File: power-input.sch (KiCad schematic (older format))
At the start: 23 parts, among them J301 Conn_01x02, J302 Conn_01x02, J303 Conn_01x02, U301 SY8401

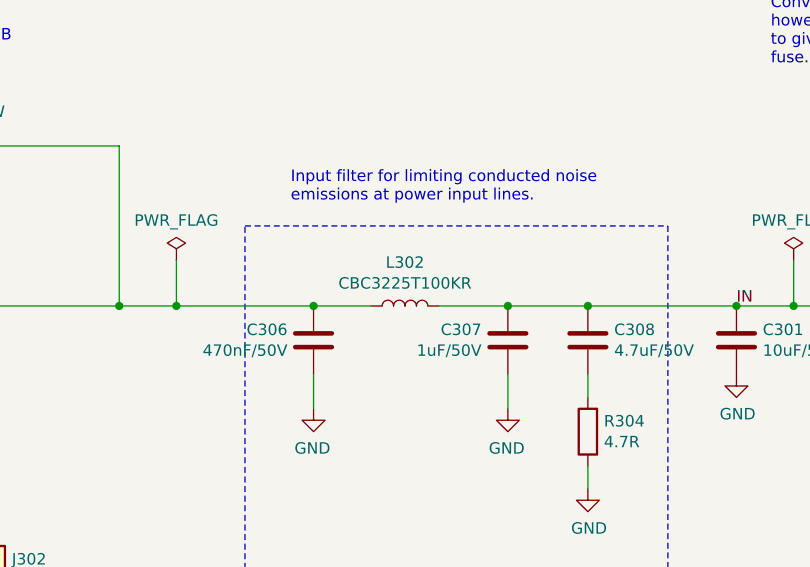
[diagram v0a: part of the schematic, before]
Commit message: Replace L302 for better availability
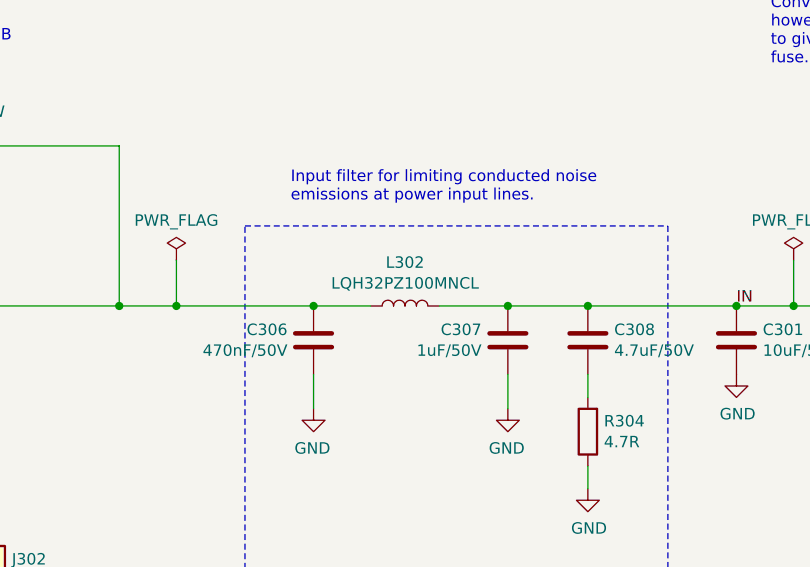
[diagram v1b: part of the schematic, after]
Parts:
- L302: value CBC3225T100KR -> LQH32PZ100MNCL; LCSC C90321 -> C464437; Notes (none) -> Alternative: CBC3225T100KR
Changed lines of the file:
@@
 AR Path="/5F6FAF6E/60159EC7" Ref="L302"  Part="1"
 F 0 "L302" V 4990 4800 50  0000 C CNN
-F 1 "CBC3225T100KR" V 4899 4800 50  0000 C CNN
+F 1 "LQH32PZ100MNCL" V 4899 4800 50  0000 C CNN
 F 2 "Inductor_SMD:L_1210_3225Metric" H 4800 4800 50  0001 C CNN
 F 3 "~" H 4800 4800 50  0001 C CNN
 F 4 "" V 4800 4800 50  0001 C CNN "URL"
 F 5 "" V 4800 4800 50  0001 C CNN "Part"
-F 6 "C90321" H 4800 4800 50  0001 C CNN "LCSC"
+F 6 "C464437" H 4800 4800 50  0001 C CNN "LCSC"
+F 7 "Alternative: CBC3225T100KR" V 4800 4800 50  0001 C CNN "Notes"
 	1    4800 4800
 	0    -1   -1   0

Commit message: Replace buck converter and CAN transceiver ICs
IC substitutions necessitated by component supply issues.
Other changes:
- Buck converter layout changes due to larger peripherals
- Isolated CAN transceiver replaced by separate digital isolators
  and transceivers. Layout changes.
- Changed JST XH conx to easier-to-use Phoenix MCs
- Removed dedicated Vin Prot conx (still available via VLink)
- Removed dedicated GND from left I/O header
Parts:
- removed C303: 100nF, Capacitor_SMD:C_0402_1005Metric, symbol Device:C
- removed C305: 10nF/50V, Capacitor_SMD:C_0402_1005Metric, symbol Device:C
- removed J302: Conn_01x02, Connector_PinHeader_2.54mm:PinHeader_1x02_P2.54mm_Vertical, symbol Connector_Generic:Conn_01x02
- removed J303: Conn_01x02, SH-ESP32:WireLink_1x02_P2.54mm, symbol Connector_Generic:Conn_01x02
- removed U301: SY8401, Package_TO_SOT_SMD:SOT-23-6, symbol SH-ESP32:SY8401
- added C201: 20nF, Capacitor_SMD:C_0402_1005Metric, symbol Device:C
- added J204: Conn_01x02, Connector_PinHeader_2.54mm:PinHeader_1x02_P2.54mm_Vertical, symbol Connector_Generic:Conn_01x02
- added U202: XL1509-ADJE1, Package_SO:SOP-8_3.9x4.9mm_P1.27mm, symbol SH-ESP32:XL1509-ADJE1
- C301: value 10uF/50V -> 22uF/35V; LCSC C13585 -> C342620; Notes 50V -> 35V
- C304: value 22uF/6.3V -> 100uF/6.3V; footprint Capacitor_SMD:C_0805_2012Metric -> Capacitor_SMD:C_1206_3216Metric; LCSC C45783 -> C15008
- D302: value B5819W -> SS24FL; footprint Diode_SMD:D_SOD-123 -> Diode_SMD:D_SOD-123F; LCSC C8598 -> C489144
- J301: footprint Connector_JST:JST_XH_B2B-XH-A_1x02_P2.50mm_Vertical -> Connector_Phoenix_MC:PhoenixContact_MCV_1,5_2-G-3.81_1x02_P3.81mm_Vertical
- L301: value MWSA0503S-100MT -> SMMS0650-470M; footprint Inductor_SMD:L_Sunlord_MWSA0518_5.4x5.2mm -> SH-ESP32:SMMS0650-1R0M; LCSC C408412 -> C149588
- L302: value LQH32PZ100MNCL -> NLCV32T-100K-PFR; LCSC C464437 -> C74563
- R302: value 68k -> 27k; LCSC C36871 -> (none)
- R303: value 15k -> 16k; LCSC C25756 -> (none)
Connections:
- net labels removed: BS
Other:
- note added: "CAN wire link"
- note added: "FB voltage divider designed to have\na 3.31V voltage at Vout.\nVfb = 1.23V"
- note removed: "CAN12V_Prot"
- note removed: "FB voltage divider designed to have\na 3.32V voltage at Vbuck"
- moved on the sheet: C304, R302

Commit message: Change CAN Vcc to 3.3V; change components for availability
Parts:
- removed C201: 20nF, Capacitor_SMD:C_0402_1005Metric, symbol Device:C
- removed R302: 27k, Resistor_SMD:R_0402_1005Metric, symbol Device:R
- removed R303: 16k, Resistor_SMD:R_0402_1005Metric, symbol Device:R
- J204: LCSC (none) -> C492401
- U202: value XL1509-ADJE1 -> XL1509-3.3; LCSC (none) -> C2681226
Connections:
- net labels removed: FB
- wire segments 59 -> 52
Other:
- note removed: "FB voltage divider designed to have\na 3.31V voltage at Vout.\nVfb = 1.23V"
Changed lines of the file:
@@
 Text Label 7700 4800 2    50   ~ 0
 SW
-Text Label 8000 5000 0    50   ~ 0
-FB
 $Comp
 L power:GND #PWR?
@@
 	1    0    0    -1
 $EndComp
-Text Notes 7950 5350 0    50   ~ 0
-FB voltage divider designed to have\na 3.31V voltage at Vout.\nVfb = 1.23V
 Wire Wire Line
 	7950 4800 7550 4800
@@
 Text Label 9250 4250 0    50   ~ 0
 Vout
-Wire Wire Line
-	9500 4250 9850 4250
 Connection ~ 9500 4250
-Connection ~ 9500 5000
-Wire Wire Line
-	9500 5000 9500 5200
-Wire Wire Line
-	9500 4700 9500 5000
-Wire Wire Line
-	7550 5000 9500 5000
-$Comp
-L Device:R R?
-U 1 1 5CA62D90
-P 9500 4550
-AR Path="/5C3476D8/5CA62D90" Ref="R?"  Part="1"
-AR Path="/5CA65CC5/5CA62D90" Ref="R?"  Part="1"
-AR Path="/5F6FAF6E/5CA62D90" Ref="R302"  Part="1"
-F 0 "R302" H 9650 4600 50  0000 C CNN
-F 1 "27k" H 9650 4500 50  0000 C CNN
-F 2 "Resistor_SMD:R_0402_1005Metric" V 9430 4550 50  0001 C CNN
-F 3 "~" H 9500 4550 50  0001 C CNN
-F 4 "" H 9500 4550 50  0001 C CNN "LCSC"
-	1    9500 4550
-	1    0    0    -1
-$EndComp
-Wire Wire Line
-	9500 4250 9500 4400
-Wire Wire Line
-	9500 5600 9500 5500
-$Comp
-L power:GND #PWR?
-U 1 1 5CA62DC4
-P 9500 5600
-AR Path="/5CA62DC4" Ref="#PWR?"  Part="1"
-AR Path="/5C3476D8/5CA62DC4" Ref="#PWR?"  Part="1"
-AR Path="/5CA65CC5/5CA62DC4" Ref="#PWR?"  Part="1"
-AR Path="/5F6FAF6E/5CA62DC4" Ref="#PWR0308"  Part="1"
-F 0 "#PWR0308" H 9500 5350 50  0001 C CNN
-F 1 "GND" H 9505 5427 50  0000 C CNN
-F 2 "" H 9500 5600 50  0001 C CNN
-F 3 "" H 9500 5600 50  0001 C CNN
-	1    9500 5600
-	1    0    0    -1
-$EndComp
-$Comp
-L Device:R R?
-U 1 1 5CA62D89
-P 9500 5350
-AR Path="/5C3476D8/5CA62D89" Ref="R?"  Part="1"
-AR Path="/5CA65CC5/5CA62D89" Ref="R?"  Part="1"
-AR Path="/5F6FAF6E/5CA62D89" Ref="R303"  Part="1"
-F 0 "R303" H 9570 5396 50  0000 L CNN
-F 1 "16k" H 9570 5305 50  0000 L CNN
-F 2 "Resistor_SMD:R_0402_1005Metric" V 9430 5350 50  0001 C CNN
-F 3 "~" H 9500 5350 50  0001 C CNN
-F 4 "" H 9500 5350 50  0001 C CNN "LCSC"
-	1    9500 5350
-	1    0    0    -1
-$EndComp
 $Comp
 L Device:D_TVS D?
@@
 P 7200 5000
 F 0 "U202" H 7200 5440 50  0000 C CNN
-F 1 "XL1509-ADJE1" H 7200 5349 50  0000 C CNN
+F 1 "XL1509-3.3" H 7200 5349 50  0000 C CNN
 F 2 "Package_SO:SOP-8_3.9x4.9mm_P1.27mm" H 7050 5000 50  0001 C CNN
 F 3 "" H 7050 5000 50  0001 C CNN
+F 4 "C2681226" H 7200 5000 50  0001 C CNN "LCSC"
 	1    7200 5000
 	1    0    0    -1
@@
 Wire Wire Line
 	6750 5000 6850 5000
-$Comp
-L Device:C C201
-U 1 1 611632AF
-P 9850 4750
-F 0 "C201" H 9965 4796 50  0000 L CNN
-F 1 "20nF" H 9965 4705 50  0000 L CNN
-F 2 "Capacitor_SMD:C_0402_1005Metric" H 9888 4600 50  0001 C CNN
-F 3 "~" H 9850 4750 50  0001 C CNN
-F 4 "" H 9850 4750 50  0001 C CNN "LCSC"
-	1    9850 4750
-	1    0    0    -1
-$EndComp
-Wire Wire Line
-	9500 5000 9850 5000
-Wire Wire Line
-	9850 5000 9850 4900
-Wire Wire Line
-	9850 4600 9850 4250
-Connection ~ 9850 4250
-Wire Wire Line
-	9850 4250 10300 4250
 Connection ~ 10300 4250
 Wire Wire Line
@@
 F 2 "Connector_PinHeader_2.54mm:PinHeader_1x02_P2.54mm_Vertical" H 1400 1500 50  0001 C CNN
 F 3 "~" H 1400 1500 50  0001 C CNN
+F 4 "C492401" H 1400 1500 50  0001 C CNN "LCSC"
 	1    1400 1500
 	-1   0    0    1
 $EndComp
+Wire Wire Line
+	9500 4250 10300 4250
+Wire Wire Line
+	9500 5000 7550 5000
+Wire Wire Line
+	9500 4250 9500 5000
 $EndSCHEMATC

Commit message: Add provisions for adjustable buck converter
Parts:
- added C201: 20nF, Capacitor_SMD:C_0402_1005Metric, symbol Device:C_Small
- added R211: 0, Resistor_SMD:R_0402_1005Metric, symbol Device:R_Small
- added R212: inf, Resistor_SMD:R_0402_1005Metric, symbol Device:R_Small
- C304: value 100uF/6.3V -> 47uF/6.3V; LCSC C15008 -> C96123
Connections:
- net labels added: FB
- wire segments 52 -> 59
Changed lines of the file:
@@
 AR Path="/5F6FAF6E/5CA62D82" Ref="C304"  Part="1"
 F 0 "C304" H 10415 4446 50  0000 L CNN
-F 1 "100uF/6.3V" H 10415 4355 50  0000 L CNN
+F 1 "47uF/6.3V" H 10415 4355 50  0000 L CNN
 F 2 "Capacitor_SMD:C_1206_3216Metric" H 10338 4250 50  0001 C CNN
 F 3 "~" H 10300 4400 50  0001 C CNN
 F 4 "Min 6.3V" H 10300 4400 50  0001 C CNN "Notes"
-F 5 "C15008" H 10300 4400 50  0001 C CNN "LCSC"
+F 5 "C96123" H 10300 4400 50  0001 C CNN "LCSC"
 	1    10300 4400
 	1    0    0    -1
@@
 	10300 4250 10550 4250
 Wire Wire Line
-	8700 4250 9500 4250
+	8700 4250 9050 4250
 $Comp
 L Connector_Generic:Conn_01x02 J204
@@
 	9500 4250 10300 4250
 Wire Wire Line
-	9500 5000 7550 5000
-Wire Wire Line
-	9500 4250 9500 5000
+	9500 5000 9050 5000
+Wire Wire Line
+	9500 4250 9500 4550
+$Comp
+L Device:R_Small R211
+U 1 1 611B9F64
+P 9500 4650
+F 0 "R211" H 9559 4696 50  0000 L CNN
+F 1 "0" H 9559 4605 50  0000 L CNN
+F 2 "Resistor_SMD:R_0402_1005Metric" H 9500 4650 50  0001 C CNN
+F 3 "~" H 9500 4650 50  0001 C CNN
+F 4 "C17168" H 9500 4650 50  0001 C CNN "LCSC"
+	1    9500 4650
+	1    0    0    -1
+$EndComp
+Wire Wire Line
+	9500 4750 9500 5000
+$Comp
+L Device:R_Small R212
+U 1 1 611BA767
+P 9500 5300
+F 0 "R212" H 9559 5346 50  0000 L CNN
+F 1 "inf" H 9559 5255 50  0000 L CNN
+F 2 "Resistor_SMD:R_0402_1005Metric" H 9500 5300 50  0001 C CNN
+F 3 "~" H 9500 5300 50  0001 C CNN
+	1    9500 5300
+	1    0    0    -1
+$EndComp
+$Comp
+L Device:C_Small C201
+U 1 1 611BAE95
+P 9050 4650
+F 0 "C201" H 9142 4696 50  0000 L CNN
+F 1 "20nF" H 9142 4605 50  0000 L CNN
+F 2 "Capacitor_SMD:C_0402_1005Metric" H 9050 4650 50  0001 C CNN
+F 3 "~" H 9050 4650 50  0001 C CNN
+F 4 "C16772" H 9050 4650 50  0001 C CNN "LCSC"
+	1    9050 4650
+	1    0    0    -1
+$EndComp
+$Comp
+L power:GND #PWR0211
+U 1 1 611BBC28
+P 9500 5550
+F 0 "#PWR0211" H 9500 5300 50  0001 C CNN
+F 1 "GND" H 9505 5377 50  0000 C CNN
+F 2 "" H 9500 5550 50  0001 C CNN
+F 3 "" H 9500 5550 50  0001 C CNN
+	1    9500 5550
+	1    0    0    -1
+$EndComp
+Wire Wire Line
+	9500 5550 9500 5400
+Wire Wire Line
+	9500 5200 9500 5000
+Connection ~ 9500 5000
+Wire Wire Line
+	9050 4750 9050 5000
+Connection ~ 9050 5000
+Wire Wire Line
+	9050 5000 7550 5000
+Wire Wire Line
+	9050 4550 9050 4250
+Connection ~ 9050 4250
+Wire Wire Line
+	9050 4250 9500 4250
+Text Label 9500 5000 0    50   ~ 0
+FB
 $EndSCHEMATC

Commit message: Fix buck FF capacitor value and part number
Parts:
- C201: value 20nF -> 22nF; LCSC C16772 -> C1532
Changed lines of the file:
@@
 P 9050 4650
 F 0 "C201" H 9142 4696 50  0000 L CNN
-F 1 "20nF" H 9142 4605 50  0000 L CNN
+F 1 "22nF" H 9142 4605 50  0000 L CNN
 F 2 "Capacitor_SMD:C_0402_1005Metric" H 9050 4650 50  0001 C CNN
 F 3 "~" H 9050 4650 50  0001 C CNN
-F 4 "C16772" H 9050 4650 50  0001 C CNN "LCSC"
+F 4 "C1532" H 9050 4650 50  0001 C CNN "LCSC"
 	1    9050 4650
 	1    0    0    -1
